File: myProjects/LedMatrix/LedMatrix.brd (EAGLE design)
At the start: 50.5 x 50.8 mm, 9 parts, among them IC1 74HC595N, IC2 74HC595N, IC3 74HC595N, IC4 ULN2803, U1 RNET, U2 RNET, X1 INPUT, X2 OUTPUT

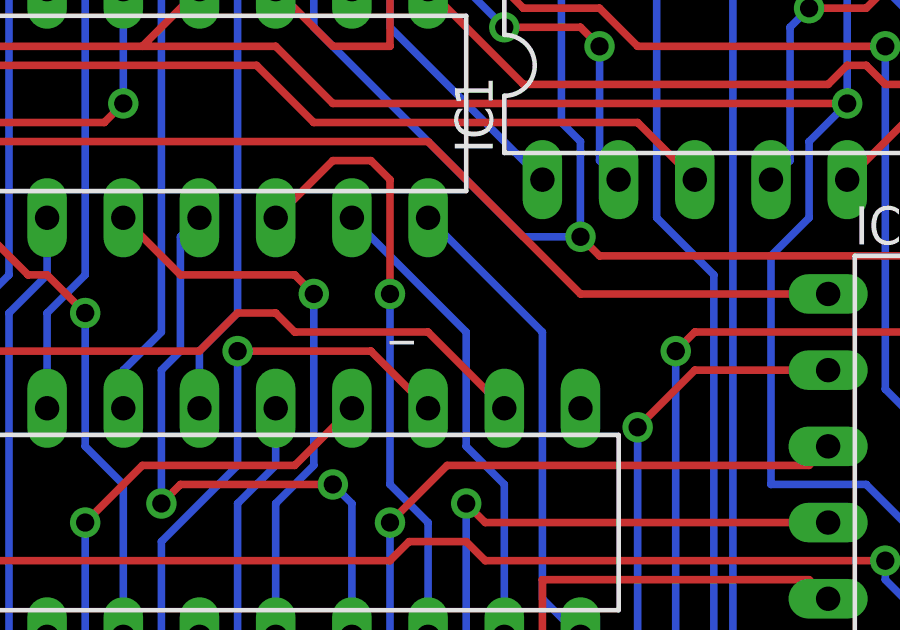
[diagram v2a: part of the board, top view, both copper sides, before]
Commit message: fixed some labelling
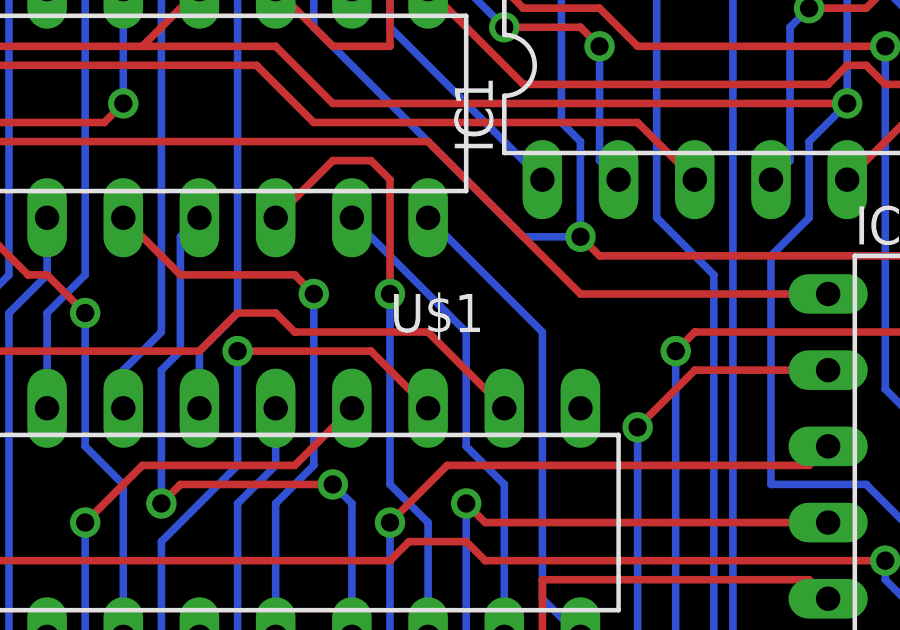
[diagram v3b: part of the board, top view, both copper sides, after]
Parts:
- renumbered _ to U$1
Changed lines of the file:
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@@
 </autorouter>
 <elements>
-<element name="_" library="led-matrix-v2" package="WLG-M2088A/8EG" value="" x="25.4" y="25.4" smashed="yes">
+<element name="U$1" library="led-matrix-v2" package="WLG-M2088A/8EG" value="" x="25.4" y="25.4" smashed="yes">
 <attribute name="NAME" x="25.4" y="25.4" size="1.27" layer="25"/>
 <attribute name="VALUE" x="25.4" y="25.4" size="1.27" layer="27"/>
@@
 <element name="IC2" library="74xx-eu" package="DIL16" value="74HC595N" x="43.815" y="17.78" rot="R270"/>
 <element name="IC3" library="74xx-eu" package="DIL16" value="74HC595N" x="17.78" y="33.02"/>
-<element name="U1" library="sibosop" package="DIP16" value="RNET" x="30.48" y="44.45"/>
+<element name="U1" library="sibosop" package="DIP16" value="RNET" x="30.48" y="44.45" smashed="yes">
+<attribute name="NAME" x="19.939" y="41.529" size="1.27" layer="25" ratio="10" rot="R90"/>
+<attribute name="VALUE" x="15.367" y="46.355" size="1.27" layer="27" ratio="10"/>
+</element>
 <element name="U2" library="sibosop" package="DIP16" value="RNET" x="22.86" y="6.35" smashed="yes" rot="MR0">
 <attribute name="NAME" x="33.401" y="3.429" size="1.27" layer="26" ratio="10" rot="MR90"/>
-<attribute name="VALUE" x="25.273" y="5.715" size="1.27" layer="27" ratio="10"/>
+<attribute name="VALUE" x="34.163" y="8.255" size="1.27" layer="27" ratio="10"/>
 </element>
 <element name="X1" library="sibosop-con-molex" package="22-23-2061" value="INPUT" x="3.81" y="36.83" smashed="yes" rot="R270">
@@
 </signal>
 <signal name="N$9">
-<contactref element="_" pad="5"/>
+<contactref element="U$1" pad="5"/>
 <contactref element="U1" pad="1"/>
 <wire x1="21.59" y1="40.64" x2="21.59" y2="44.45" width="0.254" layer="1"/>
 </signal>
 <signal name="N$10">
-<contactref element="_" pad="6"/>
+<contactref element="U$1" pad="6"/>
 <contactref element="U1" pad="2"/>
 <wire x1="24.13" y1="40.64" x2="24.13" y2="44.45" width="0.254" layer="16"/>
 </signal>
 <signal name="N$11">
-<contactref element="_" pad="7"/>
+<contactref element="U$1" pad="7"/>
 <contactref element="U1" pad="3"/>
 <wire x1="26.67" y1="40.64" x2="26.67" y2="44.45" width="0.254" layer="16"/>
 </signal>
 <signal name="N$12">
-<contactref element="_" pad="8"/>
+<contactref element="U$1" pad="8"/>
 <contactref element="U1" pad="4"/>
 <wire x1="29.21" y1="40.64" x2="29.21" y2="44.45" width="0.254" layer="16"/>
 </signal>
 <signal name="N$13">
-<contactref element="_" pad="9"/>
+<contactref element="U$1" pad="9"/>
 <contactref element="U1" pad="5"/>
 <wire x1="31.75" y1="40.64" x2="31.75" y2="44.45" width="0.254" layer="16"/>
 </signal>
 <signal name="N$14">
-<contactref element="_" pad="10"/>
+<contactref element="U$1" pad="10"/>
 <contactref element="U1" pad="6"/>
 <wire x1="34.29" y1="40.64" x2="34.29" y2="44.45" width="0.254" layer="1"/>
 </signal>
 <signal name="N$15">
-<contactref element="_" pad="11"/>
+<contactref element="U$1" pad="11"/>
 <contactref element="U1" pad="7"/>
 <wire x1="36.83" y1="40.64" x2="36.83" y2="44.45" width="0.254" layer="16"/>
 </signal>
 <signal name="N$16">
-<contactref element="_" pad="12"/>
+<contactref element="U$1" pad="12"/>
 <contactref element="U1" pad="8"/>
 <wire x1="39.37" y1="40.64" x2="39.37" y2="44.45" width="0.254" layer="16"/>
 </signal>
 <signal name="N$17">
-<contactref element="_" pad="13"/>
+<contactref element="U$1" pad="13"/>
 <contactref element="U2" pad="1"/>
 <wire x1="35.56" y1="2.54" x2="39.37" y2="6.35" width="0.254" layer="1"/>
@@
 </signal>
 <signal name="N$18">
-<contactref element="_" pad="14"/>
+<contactref element="U$1" pad="14"/>
 <contactref element="U2" pad="2"/>
 <wire x1="34.925" y1="4.445" x2="36.83" y2="6.35" width="0.254" layer="1"/>
@@
 </signal>
 <signal name="N$19">
-<contactref element="_" pad="15"/>
+<contactref element="U$1" pad="15"/>
 <contactref element="U2" pad="3"/>
 <wire x1="33.02" y1="5.08" x2="34.29" y2="6.35" width="0.254" layer="1"/>
@@
 </signal>
 <signal name="N$20">
-<contactref element="_" pad="16"/>
+<contactref element="U$1" pad="16"/>
 <contactref element="U2" pad="4"/>
 <wire x1="29.845" y1="4.445" x2="31.75" y2="6.35" width="0.254" layer="16"/>
@@
 </signal>
 <signal name="N$21">
-<contactref element="_" pad="17"/>
+<contactref element="U$1" pad="17"/>
 <contactref element="U2" pad="5"/>
 <wire x1="27.305" y1="4.445" x2="29.21" y2="6.35" width="0.254" layer="1"/>
@@
 </signal>
 <signal name="N$22">
-<contactref element="_" pad="18"/>
+<contactref element="U$1" pad="18"/>
 <contactref element="U2" pad="6"/>
 <wire x1="25.4" y1="5.08" x2="26.67" y2="6.35" width="0.254" layer="1"/>
@@
 </signal>
 <signal name="N$23">
-<contactref element="_" pad="19"/>
+<contactref element="U$1" pad="19"/>
 <contactref element="U2" pad="7"/>
 <wire x1="22.225" y1="4.445" x2="24.13" y2="6.35" width="0.254" layer="16"/>
@@
 </signal>
 <signal name="N$24">
-<contactref element="_" pad="20"/>
+<contactref element="U$1" pad="20"/>
 <contactref element="U2" pad="8"/>
 <wire x1="19.685" y1="4.445" x2="21.59" y2="6.35" width="0.254" layer="1"/>
@@
 <signal name="N$41">
 <contactref element="IC4" pad="18"/>
-<contactref element="_" pad="1"/>
+<contactref element="U$1" pad="1"/>
 <wire x1="12.7" y1="43.18" x2="11.43" y2="44.45" width="0.254" layer="16"/>
 <wire x1="12.7" y1="27.305" x2="12.7" y2="43.18" width="0.254" layer="16"/>
@@
 <signal name="N$42">
 <contactref element="IC4" pad="17"/>
-<contactref element="_" pad="2"/>
+<contactref element="U$1" pad="2"/>
 <wire x1="15.24" y1="43.18" x2="13.97" y2="44.45" width="0.254" layer="16"/>
 <wire x1="15.24" y1="27.305" x2="15.24" y2="43.18" width="0.254" layer="16"/>
@@
 <signal name="N$43">
 <contactref element="IC4" pad="16"/>
-<contactref element="_" pad="3"/>
+<contactref element="U$1" pad="3"/>
 <wire x1="17.78" y1="43.18" x2="16.51" y2="44.45" width="0.254" layer="16"/>
 <wire x1="17.78" y1="25.4" x2="17.78" y2="43.18" width="0.254" layer="16"/>
@@
 <signal name="N$44">
 <contactref element="IC4" pad="15"/>
-<contactref element="_" pad="4"/>
+<contactref element="U$1" pad="4"/>
 <wire x1="19.685" y1="43.815" x2="19.05" y2="44.45" width="0.254" layer="16"/>
 <wire x1="19.685" y1="38.735" x2="19.685" y2="43.815" width="0.254" layer="16"/>
@@
 <signal name="N$45">
 <contactref element="IC4" pad="14"/>
-<contactref element="_" pad="21"/>
+<contactref element="U$1" pad="21"/>
 <wire x1="20.32" y1="7.62" x2="19.05" y2="6.35" width="0.254" layer="16"/>
 <wire x1="20.32" y1="19.685" x2="20.32" y2="7.62" width="0.254" layer="16"/>
@@
 <signal name="N$46">
 <contactref element="IC4" pad="13"/>
-<contactref element="_" pad="22"/>
+<contactref element="U$1" pad="22"/>
 <wire x1="15.24" y1="7.62" x2="16.51" y2="6.35" width="0.254" layer="16"/>
 <wire x1="15.24" y1="19.05" x2="15.24" y2="7.62" width="0.254" layer="16"/>
@@
 <signal name="N$47">
 <contactref element="IC4" pad="12"/>
-<contactref element="_" pad="23"/>
+<contactref element="U$1" pad="23"/>
 <wire x1="15.24" y1="5.08" x2="13.97" y2="6.35" width="0.254" layer="16"/>
 <wire x1="17.78" y1="5.08" x2="15.24" y2="5.08" width="0.254" layer="16"/>
@@
 <signal name="N$48">
 <contactref element="IC4" pad="11"/>
-<contactref element="_" pad="24"/>
+<contactref element="U$1" pad="24"/>
 <wire x1="10.795" y1="6.985" x2="11.43" y2="6.35" width="0.254" layer="1"/>
 <wire x1="2.54" y1="6.985" x2="10.795" y2="6.985" width="0.254" layer="1"/>
